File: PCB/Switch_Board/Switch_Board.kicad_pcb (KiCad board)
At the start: 2 copper layers, 91.8 x 33.8 mm, 9 parts

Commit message: Updated Version_04_13
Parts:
- Main Power Switch: renamed from HV1
- Switch1: moved to B.Cu
- moved REF** 49.3 mm to (72.3, 132.2)
- moved REF** 46.5 mm to (162.2, 132.2)
- moved SolarPanel 35.4 mm to (121.5, 116.0), turned to 180 degrees
- moved REF** 31.6 mm to (72.0, 42.3)
- moved Switch1 28.5 mm to (148.8, 94.2), turned to -90 degrees
- moved REF** 27.2 mm to (161.9, 42.3)
- moved MotorController 22.6 mm to (121.4, 97.2), turned to 180 degrees
- moved LowVoltage 21.5 mm to (121.5, 76.0), turned to 180 degrees
- moved Main Power Switch 14.9 mm to (120.8, 50.5), turned to 180 degrees
- renumbered LV1 to LowVoltage, MotorController1 to MotorController, SolarPanel1 to SolarPanel
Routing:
- net Net-(LV1-A): track 16.6 -> 42.7 mm
- net Net-(MotorController1-B): track 52.4 -> 29.6 mm
- net Net-(HV1-B): track 40.6 -> 62.9 mm
- net Net-(LV1-B): track 20.9 -> 36.2 mm
- net unconnected-(LV1-C-Pad1): track 0.00 -> 0.71 mm
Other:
- board size 91.8 x 33.8 mm -> 99.8 x 99.8 mm
- board text added: "Low Voltage"
- board text added: "MAIN POWER SWITCH"
- board text added: "Motor Controller"
- board text added: "OFF"
- board text added: "ON"
- board text added: "Solar Panel"

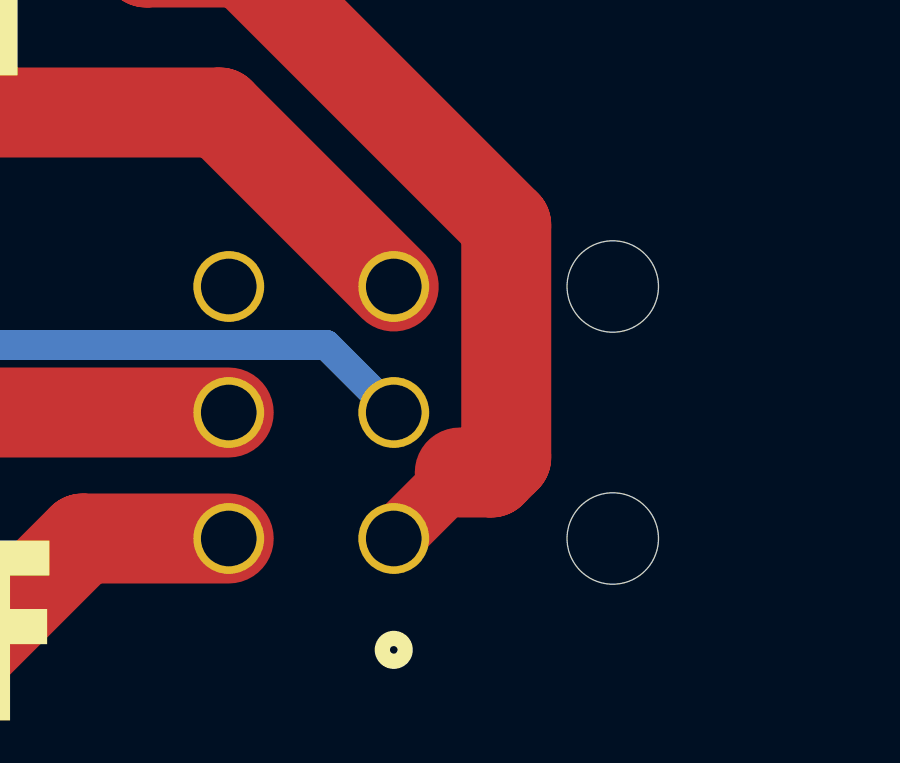
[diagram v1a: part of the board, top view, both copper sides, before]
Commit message: Change pinout to match BMS
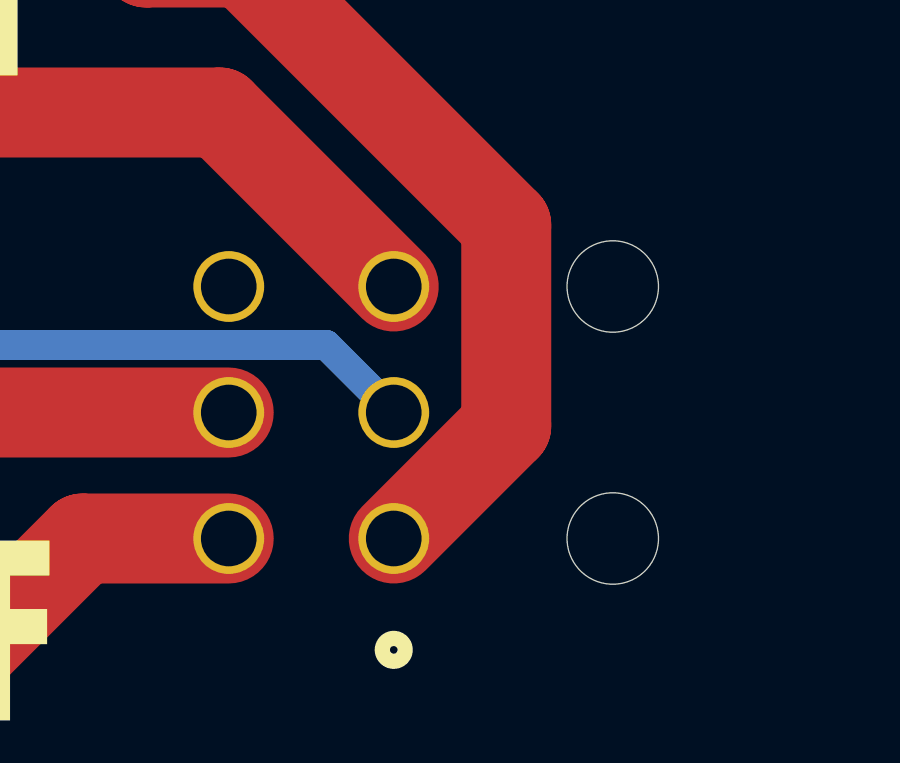
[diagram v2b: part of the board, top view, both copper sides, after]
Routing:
- net Net-(HV1-B): track 62.9 -> 62.3 mm

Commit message: Updated_Final_0418
Not including image yet, but it is the final board
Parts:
- added ESTOP1: Conn_01x02, Connector_Molex:Molex_Mini-Fit_Jr_5569-02A2_2x01_P4.20mm_Horizontal, B.Cu at (140.8, 50.3)
- added J1: Conn_01x04_Pin, Connector_Molex:Molex_Mini-Fit_Jr_5569-04A2_2x02_P4.20mm_Horizontal, B.Cu at (154.3, 82.5)
- added J4: Conn_01x04_Pin, Connector_Molex:Molex_Mini-Fit_Jr_5569-04A2_2x02_P4.20mm_Horizontal, B.Cu at (154.0, 50.3)
- added MotorControllerEN1: Conn_01x02, Connector_Molex:Molex_Mini-Fit_Jr_5569-02A2_2x01_P4.20mm_Horizontal, B.Cu at (80.4, 114.8)
- HV1: renamed from Main Power Switch
- moved MotorController1 27.2 mm to (128.7, 123.5)
- moved SolarPanel1 16.7 mm to (128.8, 101.0)
- moved HV1 16.5 mm to (106.1, 58.0)
- moved LV1 12.2 mm to (128.8, 85.8)
- moved Switch1 7.27 mm to (154.5, 98.6)
- renumbered LowVoltage to LV1, MotorController to MotorController1, SolarPanel to SolarPanel1
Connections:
- net Net-(LV1-A) renamed /LV_EN_SIGNAL
- net Net-(SolarPanel1-B) renamed /Solar_EN
- HV1 pad 2: Net-(HV1-B) -> /HV_EN
- LV1 pad 2: Net-(LV1-B) -> /LV_EN_PWR
- MotorController1 pad 3: GND -> Net-(MotorController1-A)
- Switch1 pad 1: Net-(HV1-B) -> /LV_EN_PWR
- Switch1 pad 3: Net-(LV1-B) -> /HV_EN
- Switch1 pad 5: Net-(MotorController1-B) -> /ESTOP
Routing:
- net /HV_EN: track 0.00 -> 63.2 mm
- net Net-(HV1-B): track 62.3 -> 0.00 mm
- net /ESTOP: track 0.00 -> 53.5 mm
- net Net-(MotorController1-A): track 0.00 -> 36.7 mm
- net +12V: track 0.00 -> 36.5 mm
- net Net-(LV1-B): track 36.2 -> 0.00 mm
- net /LV_EN_PWR: track 0.00 -> 35.8 mm
- net /CANH1: track 0.00 -> 28.8 mm
- net /CANL1: track 0.00 -> 22.9 mm
- net Net-(MotorController1-B): track 29.6 -> 48.7 mm
- net /Solar_EN: track 35.7 -> 28.3 mm
- net /LV_EN_SIGNAL: track 42.7 -> 40.3 mm
- net unconnected-(LV1-C-Pad1): track 0.71 -> 0.00 mm
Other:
- board text added: "(symbol "LOGO" (pin_names (offset 1.016)) (in_bom yes) (on_board yes) (property "Reference" "#G" (at 0 396.24 0) (effects (font (size 1.27 1.27)) hide) ) (property "Value" "LOGO" (at 0 -396.24 0) (effects (font (size 1.27 1.27)) hide) ) (property "Footprint" "" (at 0 0 0) (effects (font (size 1.27 1.27)) hide) ) (property "Datasheet" "" (at 0 0 0) (effects (font (size 1.27 1.27)) hide) ) (symbol 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"
- board text added: "6_PIN SWITCH"
- board text added: "CAN1"
- board text added: "CAN2"
- board text added: "ESTOP"
- board text added: "LOW VOLTAGE"
- board text added: "MAIN POWER"
- board text added: "MOTOR CONTROLLER"
- board text added: "Motor_Controller"
- board text added: "Noora Kumar | BSEE '29 | www.linkedin.com/in/noorakumar/"
- board text added: "SOLAR PANEL"

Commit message: SpritesAdded_0418
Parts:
- added G***: LOGO, LOGO, F.Cu at (85.0, 73.2)
- added G***: LOGO, LOGO, F.Cu at (106.8, 92.5)

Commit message: Updated_Images_Back_0418
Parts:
- G*** (x2): moved to B.Cu
- turned G*** to 180 degrees (x2)

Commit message: FINAL SWITCH BOARD
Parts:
- added G***: LOGO, LOGO, F.Cu at (184.8, 60.0)
